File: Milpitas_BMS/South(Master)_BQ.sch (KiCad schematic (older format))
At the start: 94 parts, among them U200 BQ79606

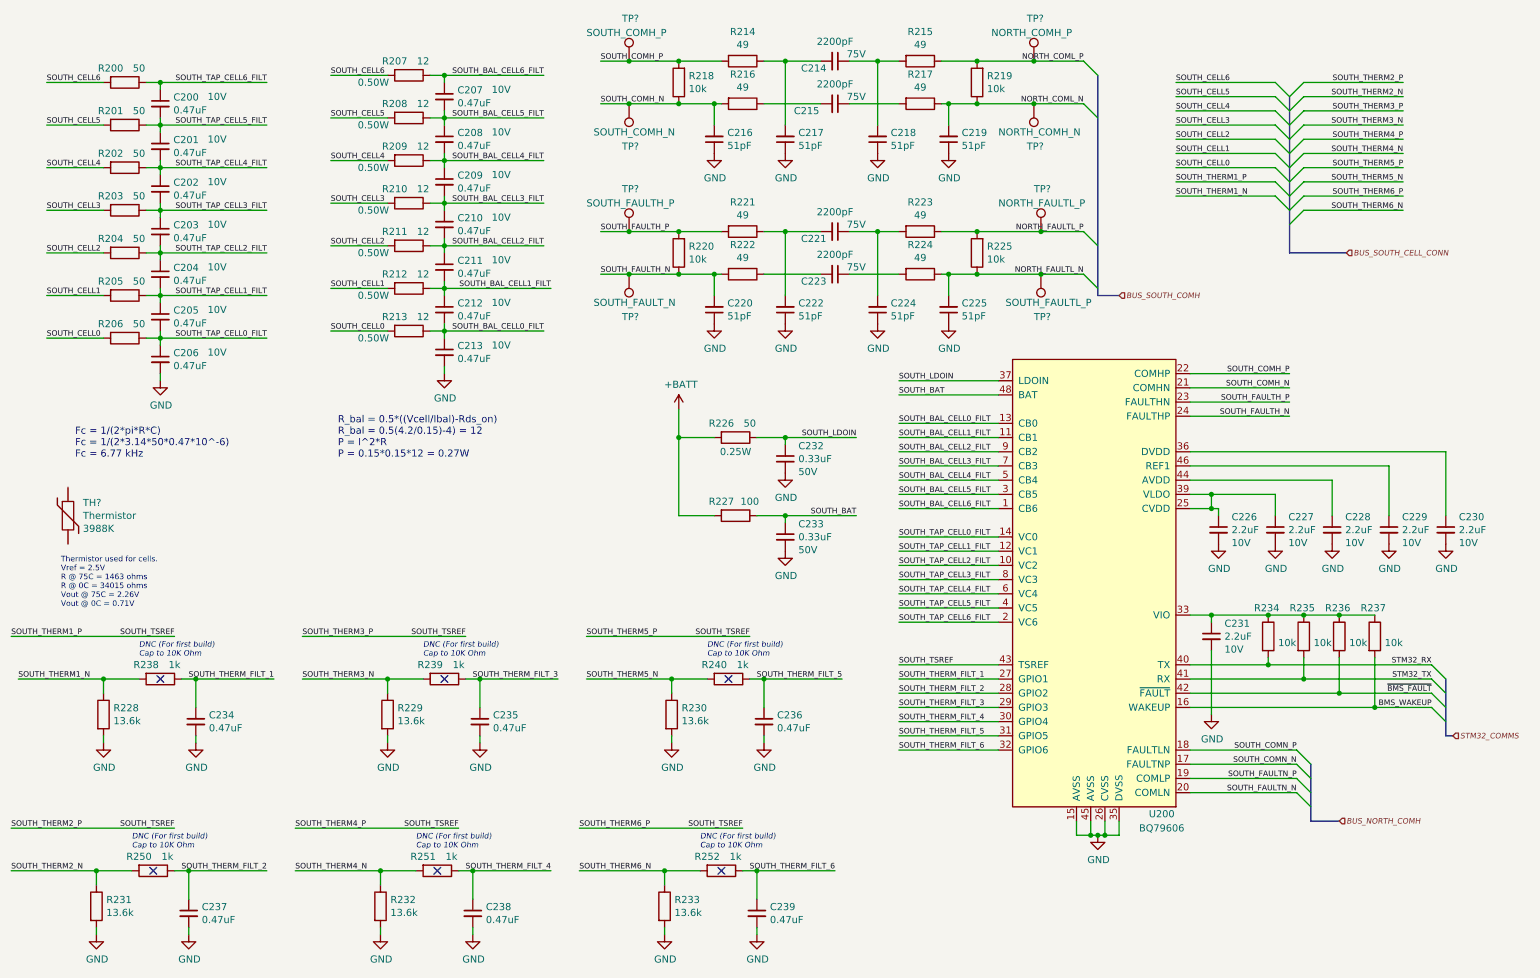
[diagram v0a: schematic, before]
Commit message: updated some parts to inclued footprints + digikey P/N
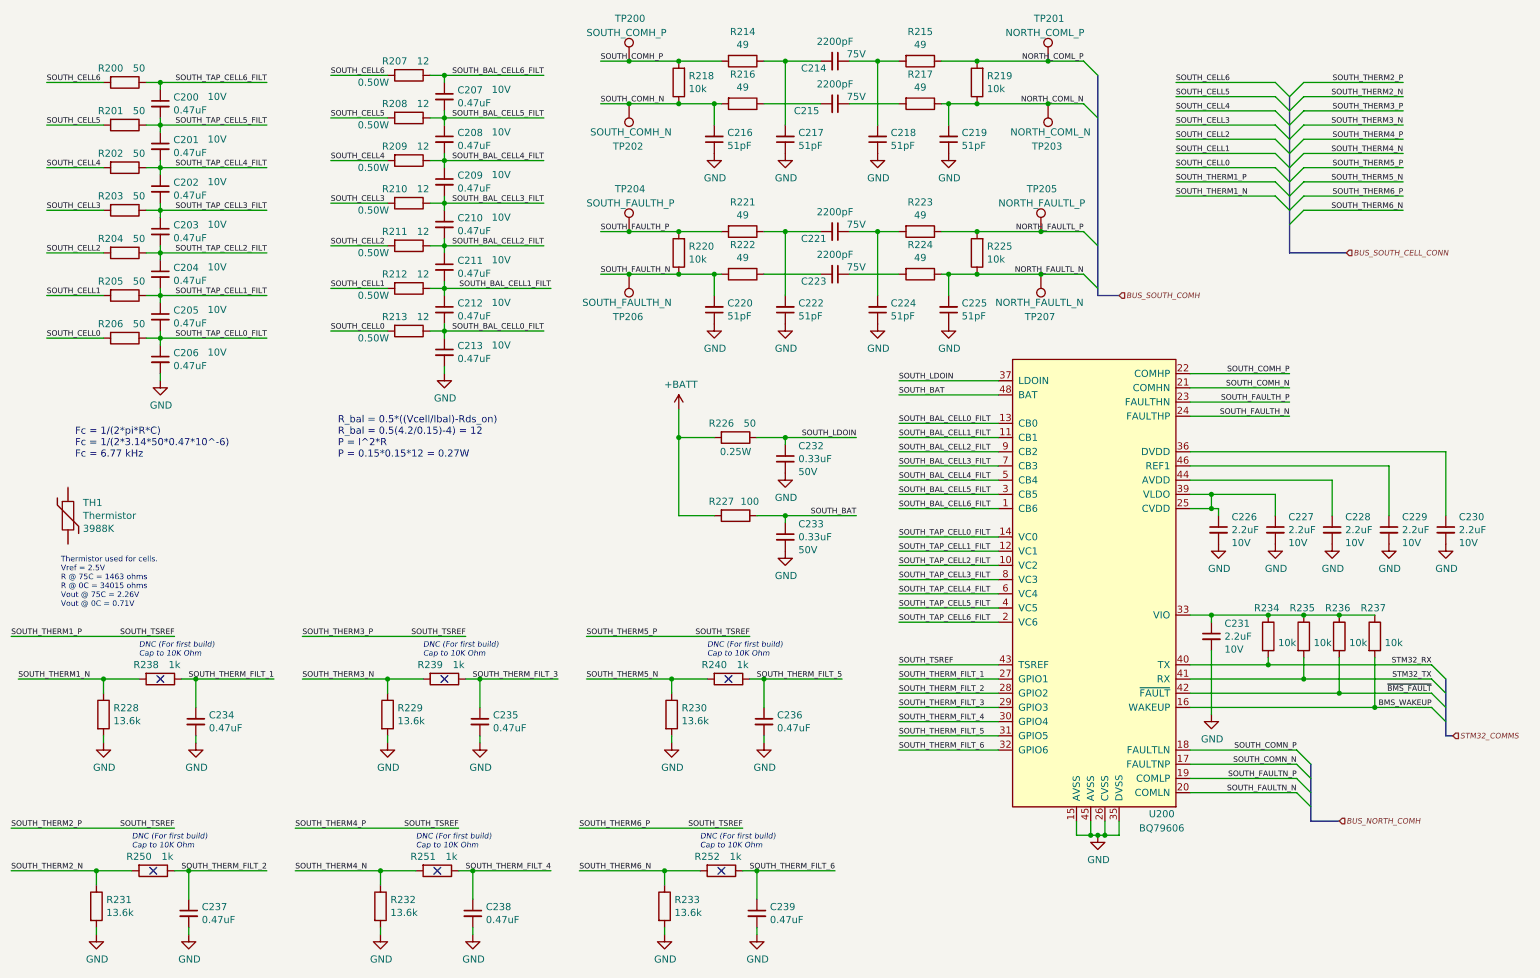
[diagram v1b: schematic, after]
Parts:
- removed TP?: SOUTH_FAULTH_P, symbol Connector:TestPoint
- removed TP?: SOUTH_FAULT_N, symbol Connector:TestPoint
- removed TP?: SOUTH_COMH_N, symbol Connector:TestPoint
- removed TP?: SOUTH_COMH_P, symbol Connector:TestPoint
- removed TP?: NORTH_COMH_P, symbol Connector:TestPoint
- removed TP?: NORTH_COMH_N, symbol Connector:TestPoint
- removed TP?: NORTH_FAULTL_P, symbol Connector:TestPoint
- removed TP?: SOUTH_FAULTL_P, symbol Connector:TestPoint
- added TP200: SOUTH_COMH_P, TestPoint:TestPoint_Bridge_Pitch2.54mm_Drill1.0mm, symbol Connector:TestPoint
- added TP201: NORTH_COML_P, TestPoint:TestPoint_Bridge_Pitch2.54mm_Drill1.0mm, symbol Connector:TestPoint
- added TP202: SOUTH_COMH_N, TestPoint:TestPoint_Bridge_Pitch2.54mm_Drill1.0mm, symbol Connector:TestPoint
- added TP203: NORTH_COML_N, TestPoint:TestPoint_Bridge_Pitch2.54mm_Drill1.0mm, symbol Connector:TestPoint
- added TP204: SOUTH_FAULTH_P, TestPoint:TestPoint_Bridge_Pitch2.54mm_Drill1.0mm, symbol Connector:TestPoint
- added TP205: NORTH_FAULTL_P, TestPoint:TestPoint_Bridge_Pitch2.54mm_Drill1.0mm, symbol Connector:TestPoint
- added TP206: SOUTH_FAULTH_N, TestPoint:TestPoint_Bridge_Pitch2.54mm_Drill1.0mm, symbol Connector:TestPoint
- added TP207: NORTH_FAULTL_N, TestPoint:TestPoint_Bridge_Pitch2.54mm_Drill1.0mm, symbol Connector:TestPoint
- C200, C201, C202, C203, C204, C205, C206, C207, C208, C209, C210, C211, C212, C213, C214, C215, C216, C217, C218, C219, C220, C221, C222, C223, C224, C225, C226, C227, C228, C229, C230, C231, C232, C233, C234, C235, C236, C237, C238, C239: footprint (none) -> Capacitor_SMD:C_0603_1608Metric
- R207, R208, R209, R210, R211, R212, R213, R214, R215, R216, R217, R218, R219, R220, R221, R222, R223, R224, R225, R226, R227, R228, R229, R230, R231, R232, R233, R234, R235, R236, R237, R238, R239, R240, R250, R251, R252: footprint (none) -> Resistor_SMD:R_0603_1608Metric
- U200: footprint (none) -> Package_QFP:LQFP-48-1EP_7x7mm_P0.5mm_EP3.6x3.6mm_ThermalVias; Digikey (none) -> 296-BQ79606APHPTQ1CT-ND
- gave numbers to parts that had none: 1
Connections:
- net NORTH_COML_N: now also TP203.1
- net NORTH_COML_P: now also TP201.1
- net NORTH_FAULTL_N: now also TP207.1
- net NORTH_FAULTL_P: now also TP205.1
- net SOUTH_COMH_N: now also TP202.1
- net SOUTH_COMH_P: now also TP200.1
- net SOUTH_FAULTH_N: now also TP206.1
- net SOUTH_FAULTH_P: now also TP204.1

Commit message: lots of little fixes
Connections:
- net SOUTH_CELL5 is gone; now on net SOUTH_CELL_5: R201.2, R208.2
- net GND: no longer C218.1, C219.1, C224.1, C225.1
- net SOUTH_CELL0 renamed SOUTH_CELL_0
- net SOUTH_CELL1 renamed SOUTH_CELL_1
- net SOUTH_CELL2 renamed SOUTH_CELL_2
- net SOUTH_CELL3 renamed SOUTH_CELL_3
- net SOUTH_CELL4 renamed SOUTH_CELL_5
- net SOUTH_CELL6 renamed SOUTH_CELL_6
- new net GNDS: C218.1, C219.1, C224.1, C225.1
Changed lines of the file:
@@
 $Comp
 L power:GND #PWR?
-U 1 1 5FC0545E
-P 6650 1500
-AR Path="/5FC0545E" Ref="#PWR?"  Part="1"
-AR Path="/5FBE719C/5FC0545E" Ref="#PWR0118"  Part="1"
-F 0 "#PWR0118" H 6650 1250 50  0001 C CNN
-F 1 "GND" H 6655 1327 50  0000 C CNN
-F 2 "" H 6650 1500 50  0001 C CNN
-F 3 "" H 6650 1500 50  0001 C CNN
-	1    6650 1500
-	1    0    0    -1
-$EndComp
-$Comp
-L power:GND #PWR?
 U 1 1 5FC05464
 P 6000 1500
@@
 $EndComp
 $Comp
-L power:GND #PWR?
-U 1 1 5FC054D8
-P 7150 1500
-AR Path="/5FC054D8" Ref="#PWR?"  Part="1"
-AR Path="/5FBE719C/5FC054D8" Ref="#PWR0121"  Part="1"
-F 0 "#PWR0121" H 7150 1250 50  0001 C CNN
-F 1 "GND" H 7155 1327 50  0000 C CNN
-F 2 "" H 7150 1500 50  0001 C CNN
-F 3 "" H 7150 1500 50  0001 C CNN
-	1    7150 1500
-	1    0    0    -1
-$EndComp
-$Comp
 L Device:R R?
 U 1 1 60146612
@@
 $Comp
 L power:GND #PWR?
-U 1 1 6023F98E
-P 6650 2700
-AR Path="/6023F98E" Ref="#PWR?"  Part="1"
-AR Path="/5FBE719C/6023F98E" Ref="#PWR0132"  Part="1"
-F 0 "#PWR0132" H 6650 2450 50  0001 C CNN
-F 1 "GND" H 6655 2527 50  0000 C CNN
-F 2 "" H 6650 2700 50  0001 C CNN
-F 3 "" H 6650 2700 50  0001 C CNN
-	1    6650 2700
-	1    0    0    -1
-$EndComp
-$Comp
-L power:GND #PWR?
 U 1 1 6023F994
 P 6000 2700
@@
 	1    0    0    -1
 $EndComp
-Text HLabel 9950 2200 2    39   Input Italic 0
-BUS_SOUTH_CELL_CONN
-Entry Wire Line
-	9650 1900 9550 2000
-Entry Wire Line
-	9650 1800 9550 1900
-Entry Wire Line
-	9650 1700 9550 1800
-Entry Wire Line
-	9650 1600 9550 1700
-Entry Wire Line
-	9650 1500 9550 1600
-Entry Wire Line
-	9650 1400 9550 1500
-Entry Wire Line
-	9650 1300 9550 1400
-Entry Wire Line
-	9650 1200 9550 1300
-Entry Wire Line
-	9650 1100 9550 1200
-Entry Wire Line
-	9650 1000 9550 1100
-Entry Wire Line
-	9450 1800 9550 1900
-Entry Wire Line
-	9450 1700 9550 1800
-Entry Wire Line
-	9450 1600 9550 1700
-Entry Wire Line
-	9450 1500 9550 1600
-Entry Wire Line
-	9450 1400 9550 1500
-Entry Wire Line
-	9450 1300 9550 1400
-Entry Wire Line
-	9450 1200 9550 1300
-Entry Wire Line
-	9450 1100 9550 1200
-Entry Wire Line
-	9450 1000 9550 1100
-Text Label 10350 1900 2    39   ~ 0
+Text Label 9450 2500 0    39   ~ 0
 SOUTH_THERM6_N
-Text Label 10350 1800 2    39   ~ 0
+Text Label 9450 2400 0    39   ~ 0
 SOUTH_THERM6_P
 Wire Wire Line
-	10350 1900 9650 1900
+	9450 2500 10150 2500
 Wire Wire Line
-	10350 1800 9650 1800
-Text Label 10350 1700 2    39   ~ 0
+	9450 2400 10150 2400
+Text Label 9450 2300 0    39   ~ 0
 SOUTH_THERM5_N
-Text Label 10350 1600 2    39   ~ 0
+Text Label 9450 2200 0    39   ~ 0
 SOUTH_THERM5_P
 Wire Wire Line
-	10350 1700 9650 1700
+	9450 2300 10150 2300
 Wire Wire Line
-	10350 1600 9650 1600
-Text Label 10350 1500 2    39   ~ 0
+	9450 2200 10150 2200
+Text Label 9450 2100 0    39   ~ 0
 SOUTH_THERM4_N
-Text Label 10350 1400 2    39   ~ 0
+Text Label 9450 2000 0    39   ~ 0
 SOUTH_THERM4_P
 Wire Wire Line
-	10350 1500 9650 1500
+	9450 2100 10150 2100
 Wire Wire Line
-	10350 1400 9650 1400
-Text Label 10350 1300 2    39   ~ 0
+	9450 2000 10150 2000
+Text Label 9450 1900 0    39   ~ 0
 SOUTH_THERM3_N
-Text Label 10350 1200 2    39   ~ 0
+Text Label 9450 1800 0    39   ~ 0
 SOUTH_THERM3_P
 Wire Wire Line
-	10350 1300 9650 1300
+	9450 1900 10150 1900
 Wire Wire Line
-	10350 1200 9650 1200
-Text Label 10350 1100 2    39   ~ 0
+	9450 1800 10150 1800
+Text Label 9450 1700 0    39   ~ 0
 SOUTH_THERM2_N
-Text Label 10350 1000 2    39   ~ 0
+Text Label 9450 1600 0    39   ~ 0
 SOUTH_THERM2_P
 Wire Wire Line
-	10350 1100 9650 1100
+	9450 1700 10150 1700
 Wire Wire Line
-	10350 1000 9650 1000
-Text Label 8750 1800 0    39   ~ 0
+	9450 1600 10150 1600
+Text Label 9450 1500 0    39   ~ 0
 SOUTH_THERM1_N
-Text Label 8750 1700 0    39   ~ 0
+Text Label 9450 1400 0    39   ~ 0
 SOUTH_THERM1_P
 Wire Wire Line
-	8750 1800 9450 1800
+	9450 1500 10150 1500
 Wire Wire Line
-	8750 1700 9450 1700
-Text Label 8750 1000 0    39   ~ 0
+	9450 1400 10150 1400
+Text Label 9450 700  0    39   ~ 0
 SOUTH_CELL6
-Text Label 8750 1100 0    39   ~ 0
+Text Label 9450 800  0    39   ~ 0
 SOUTH_CELL5
-Text Label 8750 1200 0    39   ~ 0
+Text Label 9450 900  0    39   ~ 0
 SOUTH_CELL4
-Text Label 8750 1300 0    39   ~ 0
+Text Label 9450 1000 0    39   ~ 0
 SOUTH_CELL3
-Text Label 8750 1400 0    39   ~ 0
+Text Label 9450 1100 0    39   ~ 0
 SOUTH_CELL2
-Text Label 8750 1500 0    39   ~ 0
+Text Label 9450 1200 0    39   ~ 0
 SOUTH_CELL1
-Text Label 8750 1600 0    39   ~ 0
+Text Label 9450 1300 0    39   ~ 0
 SOUTH_CELL0
 Wire Wire Line
-	8750 1600 9450 1600
+	9450 1300 10150 1300
 Wire Wire Line
-	8750 1500 9450 1500
+	9450 1200 10150 1200
 Wire Wire Line
-	8750 1400 9450 1400
+	9450 1100 10150 1100
 Wire Wire Line
-	8750 1300 9450 1300
+	9450 1000 10150 1000
 Wire Wire Line
-	8750 1200 9450 1200
+	9450 900  10150 900
 Wire Wire Line
-	8750 1100 9450 1100
+	9450 800  10150 800
 Wire Wire Line
-	8750 1000 9450 1000
+	9450 700  10150 700
 Text Label 4700 2050 0    39   ~ 0
 SOUTH_FAULTH_P
@@
 Text HLabel 8350 2500 2    39   Input Italic 0
 BUS_SOUTH_COMH
-Wire Bus Line
-	9550 2200 9950 2200
 Text Label 9550 3050 2    39   ~ 0
 SOUTH_COMH_P
@@
 	7100 2350 7150 2350
 $Comp
-L power:GND #PWR?
-U 1 1 6023F9D2
-P 7150 2700
-AR Path="/6023F9D2" Ref="#PWR?"  Part="1"
-AR Path="/5FBE719C/6023F9D2" Ref="#PWR0136"  Part="1"
-F 0 "#PWR0136" H 7150 2450 50  0001 C CNN
-F 1 "GND" H 7155 2527 50  0000 C CNN
-F 2 "" H 7150 2700 50  0001 C CNN
-F 3 "" H 7150 2700 50  0001 C CNN
-	1    7150 2700
-	1    0    0    -1
-$EndComp
-$Comp
 L Device:C_Small C?
 U 1 1 6023F9BA
@@
 	-1   0    0    1
 $EndComp
+Connection ~ 7800 2350
+Wire Wire Line
+	7800 2350 8100 2350
+$Comp
+L power:GNDS #PWR0132
+U 1 1 5E8619DB
+P 6650 1500
+F 0 "#PWR0132" H 6650 1250 50  0001 C CNN
+F 1 "GNDS" H 6655 1327 50  0000 C CNN
+F 2 "" H 6650 1500 50  0001 C CNN
+F 3 "" H 6650 1500 50  0001 C CNN
+	1    6650 1500
+	1    0    0    -1
+$EndComp
+$Comp
+L power:GNDS #PWR0136
+U 1 1 5E861EE3
+P 7150 1500
+F 0 "#PWR0136" H 7150 1250 50  0001 C CNN
+F 1 "GNDS" H 7155 1327 50  0000 C CNN
+F 2 "" H 7150 1500 50  0001 C CNN
+F 3 "" H 7150 1500 50  0001 C CNN
+	1    7150 1500
+	1    0    0    -1
+$EndComp
+$Comp
+L power:GNDS #PWR0205
+U 1 1 5E8621B4
+P 6650 2700
+F 0 "#PWR0205" H 6650 2450 50  0001 C CNN
+F 1 "GNDS" H 6655 2527 50  0000 C CNN
+F 2 "" H 6650 2700 50  0001 C CNN
+F 3 "" H 6650 2700 50  0001 C CNN
+	1    6650 2700
+	1    0    0    -1
+$EndComp
+Text GLabel 10150 700  2    39   Input ~ 0
+SOUTH_CELL_6
+Text GLabel 10150 800  2    39   Input ~ 0
+SOUTH_CELL_5
+Text GLabel 10150 900  2    39   Input ~ 0
+SOUTH_CELL_5
+Text GLabel 10150 1000 2    39   Input ~ 0
+SOUTH_CELL_3
+Text GLabel 10150 1100 2    39   Input ~ 0
+SOUTH_CELL_2
+Text GLabel 10150 1200 2    39   Input ~ 0
+SOUTH_CELL_1
+Text GLabel 10150 1300 2    39   Input ~ 0
+SOUTH_CELL_0
+Text GLabel 10150 1400 2    39   Input ~ 0
+SOUTH_THERM1_P
+Text GLabel 10150 1500 2    39   Input ~ 0
+SOUTH_THERM1_N
+Text GLabel 10150 1600 2    39   Input ~ 0
+SOUTH_THERM2_P
+Text GLabel 10150 1800 2    39   Input ~ 0
+SOUTH_THERM3_P
+Text GLabel 10150 1900 2    39   Input ~ 0
+SOUTH_THERM3_N
+Text GLabel 10150 2000 2    39   Input ~ 0
+SOUTH_THERM4_P
+Text GLabel 10150 2100 2    39   Input ~ 0
+SOUTH_THERM4_N
+Text GLabel 10150 2200 2    39   Input ~ 0
+SOUTH_THERM5_P
+Text GLabel 10150 2300 2    39   Input ~ 0
+SOUTH_THERM5_N
+Text GLabel 10150 2400 2    39   Input ~ 0
+SOUTH_THERM6_P
+Text GLabel 10150 2500 2    39   Input ~ 0
+SOUTH_THERM6_N
+Text GLabel 10150 1700 2    39   Input ~ 0
+SOUTH_THERM2_N
+$Comp
+L power:GNDS #PWR0206
+U 1 1 5E862586
+P 7150 2700
+F 0 "#PWR0206" H 7150 2450 50  0001 C CNN
+F 1 "GNDS" H 7155 2527 50  0000 C CNN
+F 2 "" H 7150 2700 50  0001 C CNN
+F 3 "" H 7150 2700 50  0001 C CNN
+	1    7150 2700
+	1    0    0    -1
+$EndComp
 Wire Bus Line
 	10650 5200 10650 5600
@@
 Wire Bus Line
 	8200 950  8200 2500
-Wire Bus Line
-	9550 1100 9550 2200
-Connection ~ 7800 2350
-Wire Wire Line
-	7800 2350 8100 2350
 $EndSCHEMATC

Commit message: For review call
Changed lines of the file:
@@
 Wire Wire Line
 	8850 3350 9550 3350
-Entry Wire Line
-	8100 850  8200 950
-Entry Wire Line
-	8100 1150 8200 1250
-Entry Wire Line
-	8100 2050 8200 2150
-Entry Wire Line
-	8100 2350 8200 2450
-Wire Bus Line
-	8200 2500 8350 2500
-Text HLabel 8350 2500 2    39   Input Italic 0
-BUS_SOUTH_COMH
 Text Label 9550 3050 2    39   ~ 0
 SOUTH_COMH_P
@@
 Text Label 9600 6000 2    39   ~ 0
 SOUTH_FAULTN_N
-Entry Wire Line
-	9600 5700 9700 5800
-Entry Wire Line
-	9600 5800 9700 5900
-Entry Wire Line
-	9600 5900 9700 6000
-Entry Wire Line
-	9600 6000 9700 6100
-Wire Bus Line
-	9700 6200 9900 6200
-Text HLabel 9900 6200 2    39   Input Italic 0
-BUS_NORTH_COMH
-Entry Wire Line
-	10550 5100 10650 5200
-Entry Wire Line
-	10550 5200 10650 5300
-Entry Wire Line
-	10550 5300 10650 5400
-Entry Wire Line
-	10550 5400 10650 5500
-Wire Bus Line
-	10650 5600 10700 5600
-Text HLabel 10700 5600 2    39   Input Italic 0
-STM32_COMMS
 Text Label 550  4900 0    39   ~ 0
 SOUTH_THERM1_P
@@
 	1    0    0    -1
 $EndComp
-Wire Bus Line
-	10650 5200 10650 5600
-Wire Bus Line
-	9700 5800 9700 6200
-Wire Bus Line
-	8200 950  8200 2500
+Text GLabel 10550 5100 2    39   Input ~ 0
+STM32_RX
+Text GLabel 10550 5200 2    39   Input ~ 0
+STM32_TX
+Text GLabel 10550 5300 2    39   Input ~ 0
+~BMS_FAULT
+Text GLabel 10550 5400 2    39   Input ~ 0
+BMS_WAKEUP
+Text GLabel 8100 850  2    39   Input ~ 0
+NORTH_COML_P
+Text GLabel 8100 1150 2    39   Input ~ 0
+NORTH_COML_N
+Text GLabel 8100 2050 2    39   Input ~ 0
+NORTH_FAULTL_P
+Text GLabel 8100 2350 2    39   Input ~ 0
+NORTH_FAULTL_N
+Text GLabel 9600 5700 2    39   Input ~ 0
+SOUTH_COMN_P
+Text GLabel 9600 5800 2    39   Input ~ 0
+SOUTH_COMN_N
+Text GLabel 9600 5900 2    39   Input ~ 0
+SOUTH_FAULTN_P
+Text GLabel 9600 6000 2    39   Input ~ 0
+SOUTH_FAULTN_N
 $EndSCHEMATC

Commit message: prelim layout ???
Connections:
- net SOUTH_CELL_5: no longer R202.2, R209.2
- new net SOUTH_CELL_4: R202.2, R209.2
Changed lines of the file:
@@
 SOUTH_CELL_5
 Text GLabel 10150 900  2    39   Input ~ 0
-SOUTH_CELL_5
+SOUTH_CELL_4
 Text GLabel 10150 1000 2    39   Input ~ 0
 SOUTH_CELL_3

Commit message: (maybe) final placement V1,0
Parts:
- removed TP200: SOUTH_COMH_P, TestPoint:TestPoint_Bridge_Pitch2.54mm_Drill1.0mm, symbol Connector:TestPoint
- removed TP201: NORTH_COML_P, TestPoint:TestPoint_Bridge_Pitch2.54mm_Drill1.0mm, symbol Connector:TestPoint
- removed TP202: SOUTH_COMH_N, TestPoint:TestPoint_Bridge_Pitch2.54mm_Drill1.0mm, symbol Connector:TestPoint
- removed TP203: NORTH_COML_N, TestPoint:TestPoint_Bridge_Pitch2.54mm_Drill1.0mm, symbol Connector:TestPoint
- removed TP204: SOUTH_FAULTH_P, TestPoint:TestPoint_Bridge_Pitch2.54mm_Drill1.0mm, symbol Connector:TestPoint
- removed TP205: NORTH_FAULTL_P, TestPoint:TestPoint_Bridge_Pitch2.54mm_Drill1.0mm, symbol Connector:TestPoint
- removed TP206: SOUTH_FAULTH_N, TestPoint:TestPoint_Bridge_Pitch2.54mm_Drill1.0mm, symbol Connector:TestPoint
- removed TP207: NORTH_FAULTL_N, TestPoint:TestPoint_Bridge_Pitch2.54mm_Drill1.0mm, symbol Connector:TestPoint
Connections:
- net +BATT is gone; now on net SOUTH_CELL_6: R226.2, R227.2
- net S_COMH_LS_P: now reaches C214.1, C218.2, R215.2
- net S_COMH_LS_N: now reaches C215.1, R217.2
- net S_FAULTH_LS_P: now reaches C221.1, C224.2, R223.2
- net S_FAULTH_LS_N: now reaches C223.1, R224.2
- net STM32_RX renamed STM32_UART_P
- net STM32_TX renamed STM32_UART_N
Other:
- note added: "Refrenced off the highest in the local cell stack"
- moved on the sheet: R223, R224
